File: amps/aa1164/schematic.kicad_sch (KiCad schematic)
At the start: 95 parts, among them SW1 SPST, SW2 SPDT

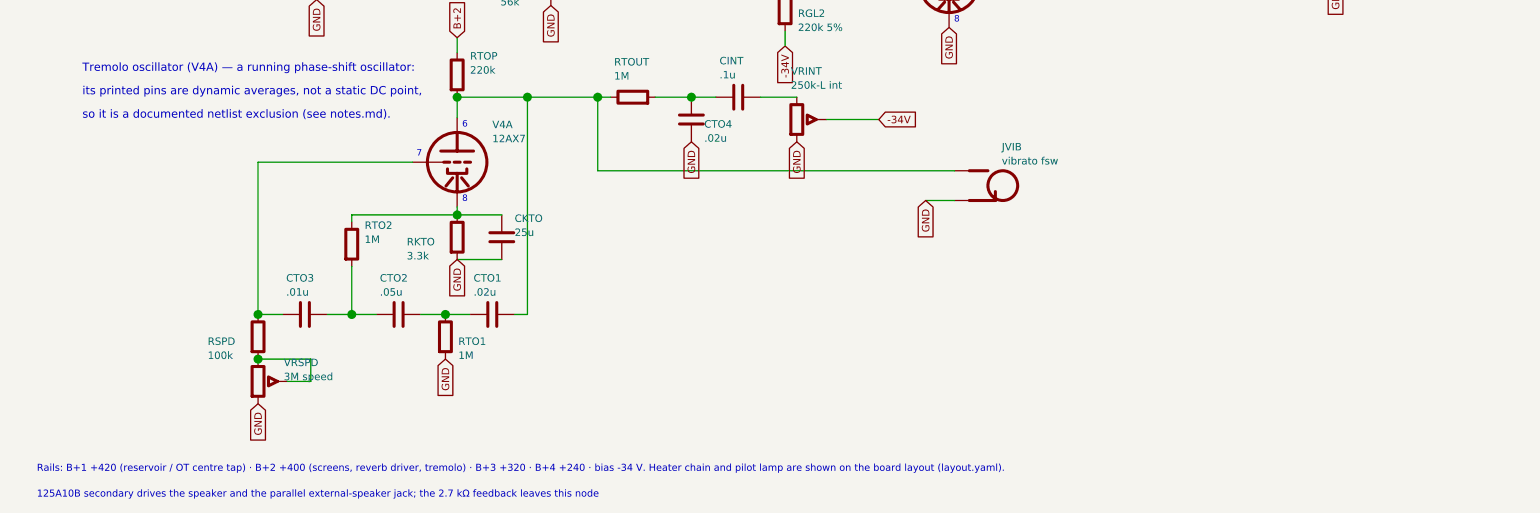
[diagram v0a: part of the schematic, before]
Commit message: Fix: schematic sheet notes no longer name repository files
Thirty-seven committed sheets rendered footnotes and section notes such as
"Heaters and PT primary omitted — see netlist.cir and meta.yaml" or
"excluded from netlist.cir (notes.md)" to visitors through KiCanvas. The
prose sweeps never counted sheets. Rewritten in the site's own words — the
netlist, the sources list, the circuit story, the parts list, the board
drawing — in 59 strings across 33 draw scripts, keeping every technical
claim as it was; the three tone sheets (6G4, 6G5, 6G6-B) are under repair
elsewhere and keep theirs for now. The sweep touched only strings passed to
the sheet's note, text, caption and footnote calls, never a path or a value.

Gates: check_schematics 40/0, connectivity 0 isolated pins;
verify_schematic_nets 40 clean; only the regenerated sheets and their served
copies changed.

Co-Authored-By: Claude Fable 5.1 <noreply@anthropic.com>
Claude-Session: https://claude.ai/code/session_01KBMfdh37HmCL2iWcBiL5J1
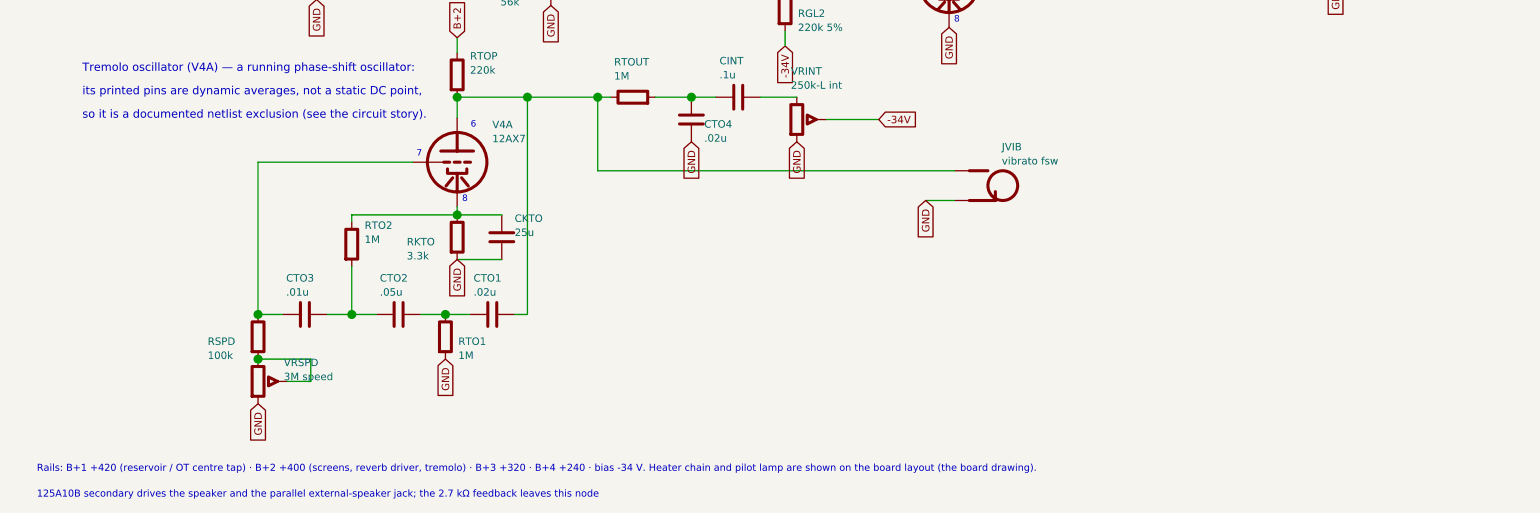
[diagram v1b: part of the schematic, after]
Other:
- note added: "Rails: B+1 +420 (reservoir / OT centre tap) · B+2 +400 (screens, reverb driver, tremolo) · B+3 +320 · B+4 +240 · bias -34 V. Heater chain and pilot lamp are shown on the board layout (the board drawing)."
- note added: "so it is a documented netlist exclusion (see the circuit story)."
- note removed: "Rails: B+1 +420 (reservoir / OT centre tap) · B+2 +400 (screens, reverb driver, tremolo) · B+3 +320 · B+4 +240 · bias -34 V. Heater chain and pilot lamp are shown on the board layout (layout.yaml)."
- note removed: "so it is a documented netlist exclusion (see notes.md)."
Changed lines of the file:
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@@
   (text "its printed pins are dynamic averages, not a static DC point," (at 20.4724 222.75 0)
     (effects (font (size 1.4 1.4)) (justify left)))
-  (text "so it is a documented netlist exclusion (see notes.md)." (at 20.4724 226.75 0)
+  (text "so it is a documented netlist exclusion (see the circuit story)." (at 20.4724 226.75 0)
     (effects (font (size 1.4 1.4)) (justify left)))
   (symbol (lib_id "cx:TRIODE") (at 84.4724 234.75 0) (unit 1)
@@
   (text "8" (at 169.322 210.465 0)
     (effects (font (size 1.1 1.1)) (justify left)))
-  (text "6" (at 85.3224 228.4 0)
+  (text "6" (at 86.7724 228.4 0)
     (effects (font (size 1.1 1.1)) (justify left)))
   (text "7" (at 77.5252 233.35 0)
@@
   (text "8" (at 85.3224 241.1 0)
     (effects (font (size 1.1 1.1)) (justify left)))
-  (text "Rails: B+1 +420 (reservoir / OT centre tap) · B+2 +400 (screens, reverb driver, tremolo) · B+3 +320 · B+4 +240 · bias -34 V. Heater chain and pilot lamp are shown on the board layout (layout.yaml)." (at 12.7 287.148 0)
+  (text "Rails: B+1 +420 (reservoir / OT centre tap) · B+2 +400 (screens, reverb driver, tremolo) · B+3 +320 · B+4 +240 · bias -34 V. Heater chain and pilot lamp are shown on the board layout (the board drawing)." (at 12.7 287.148 0)
     (effects (font (size 1.2 1.2)) (justify left)))
   (text "125A10B secondary drives the speaker and the parallel external-speaker jack; the 2.7 kΩ feedback leaves this node" (at 12.7 291.548 0)

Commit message: Fix: state the datasheet unit on 17 dual-triode sections whose sheets printed the other half's pin numbers
The sheet-vs-board gate reported these sockets as SECTION-SWAP; the
2026-09-10 source-read triage found the BOARD right on every one of them
(and both surfaces wrong on the 5G9 tremolo bottle). Each sheet had
lettered the section on the default map (A -> unit 1 -> pins 6/7/8) where
the factory drawing puts that stage on 1/2/3. The draw scripts now state
`unit=` on both halves, with the source cited beside the call, so the
printed socket numbers are the factory's:

- 5f4 V3: driver V3A -> 1/2/3, cathodyne V3B -> 6/7/8
  (crop 5f4-V3-layout-trace.png: +213 V driver plate -> pin 1, +270 V -> 6)
- 5f8a V3: 82k half V3A -> 1/2/3, 100k half V3B -> 6/7/8
  (crop 5f8a-V3-layout-trace.png: +225 -> 6, +19 -> 2, +28.5 -> 8)
- 6161 V1: channel 1 V1A -> 1/2/3 (crop 6161-V1-ch1.png prints 1/2/3);
  6161 V2: 1 MEG-grid half V2A -> 1/2/3, paraphase V2B -> 6/7/8
  (crop 6161-V2.png / 6161-V2-right.png)
- 6g3 V3: 82k half V3A -> 1/2/3 (crop 6g3-V3-layout-wires.png: +230 -> 1,
  +225 -> 6, +20 -> 7)
- aa1164 V3: recovery V3A -> 1/2/3, mixer V3B -> 6/7/8
  (crops aa1164-V3A-recovery-schem.png, aa1164-V3B-mixer-schem.png)
- aa864-bassman V1/V2: input stages 2/1/3, second stages 7/6/8; V4: the
  .1/500 pF-fed 82k half 2/1/3 (crops aa864-V1A-input.png,
  aa864-V1B-second.png, aa864-V2A-input.png, aa864-V2B-second.png,
  aa864-V4-PI.png)
- ab165 V1/V2/V4: same pattern (crops ab165-V1A-input.png,
  ab165-V1B-second.png, ab165-V2A-input.png, ab165-V2B-second.png,
  ab165-V4-PI.png)
- ab763-super V1/V2: slope-plate +270 V -> pin 1 (input stage), .047
  plate -> 6 (crops ab763-super-V1-layout-sh.png, ab763-super-V2-layout-sh.png)
- dr103 V2/V3: gain stages 6/7/8, cathode followers 1/2/3 (crops
  dr103-V2-huss.png, dr103-V3-huss.png — the Huss redraw, not a factory
  print; noted in the script)
- 5g9 V3: oscillator V3A -> 1/2/3, follower V3B -> 6/7/8 (crops
  5g9-V3-strap71-zoom.png, 5g9-V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
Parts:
- V3A: Basing_unit (none) -> 2
- V3B: Basing_unit (none) -> 1
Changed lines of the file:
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@@
     (in_bom yes) (on_board yes)
     (property "Reference" "V3A" (at 150.472 98.35 0) (effects (font (size 1.27 1.27)) (justify left)))
-    (property "Value" "12AX7" (at 150.472 100.75 0) (effects (font (size 1.27 1.27)) (justify left))))
+    (property "Value" "12AX7" (at 150.472 100.75 0) (effects (font (size 1.27 1.27)) (justify left)))
+    (property "Basing_unit" "2" (at 150.472 103.15 0) (effects (font (size 1.27 1.27)) hide)))
   (wire (pts (xy 132.472 104.75) (xy 136.852 104.75))
     (stroke (width 0) (type default)))
@@
     (in_bom yes) (on_board yes)
     (property "Reference" "V3B" (at 66.4724 176.35 0) (effects (font (size 1.27 1.27)) (justify left)))
-    (property "Value" "12AX7" (at 66.4724 178.75 0) (effects (font (size 1.27 1.27)) (justify left))))
+    (property "Value" "12AX7" (at 66.4724 178.75 0) (effects (font (size 1.27 1.27)) (justify left)))
+    (property "Basing_unit" "1" (at 66.4724 181.15 0) (effects (font (size 1.27 1.27)) hide)))
   (wire (pts (xy 44.4724 182.75) (xy 52.8524 182.75))
     (stroke (width 0) (type default)))
@@
   (text "3" (at 55.3224 133.1 0)
     (effects (font (size 1.1 1.1)) (justify left)))
-  (text "6" (at 145.322 98.4 0)
-    (effects (font (size 1.1 1.1)) (justify left)))
-  (text "7" (at 137.525 103.35 0)
-    (effects (font (size 1.1 1.1)) (justify left)))
-  (text "8" (at 145.322 111.1 0)
-    (effects (font (size 1.1 1.1)) (justify left)))
-  (text "1" (at 61.3224 176.4 0)
-    (effects (font (size 1.1 1.1)) (justify left)))
-  (text "2" (at 53.5252 181.35 0)
-    (effects (font (size 1.1 1.1)) (justify left)))
-  (text "3" (at 61.3224 189.1 0)
+  (text "1" (at 145.322 98.4 0)
+    (effects (font (size 1.1 1.1)) (justify left)))
+  (text "2" (at 137.525 103.35 0)
+    (effects (font (size 1.1 1.1)) (justify left)))
+  (text "3" (at 145.322 111.1 0)
+    (effects (font (size 1.1 1.1)) (justify left)))
+  (text "6" (at 61.3224 176.4 0)
+    (effects (font (size 1.1 1.1)) (justify left)))
+  (text "7" (at 53.5252 181.35 0)
+    (effects (font (size 1.1 1.1)) (justify left)))
+  (text "8" (at 61.3224 189.1 0)
     (effects (font (size 1.1 1.1)) (justify left)))
   (text "1" (at 101.322 176.4 0)

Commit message: Fix: 17 bias rectifiers and six HT diodes drawn backwards; the 6G6-B and 6G4 bias rows as their drawings show; AA1164 V4 units
Rectifier polarity has no gate. The netlists model every supply as an ideal
source, the sheet-vs-board check treats a two-terminal part as unordered, and
the boards' `cathode:` fields were copied from the sheets. Measured over all
68 diodes on 40 sheets: 18 negative-bias rectifiers had the cathode on the
negative node (a diode that way round would charge the node POSITIVE), and all
six 6G6-B HT diodes pointed away from B+. The printed negative bias on each of
those sheets falsifies the drawn orientation; the nine bias rectifiers already
right (AA1164, AA864, AB165, B15N, DR103, JTM100, M1959, M2204, 6G6-B) show
the idiom. Flipped: 5E4-A, 5E5-A, 5E6-A, 5F10, 5F4, 5F6, 5F6-A, 5F8-A, 5G9,
6G2, 6G3, 6G4, 6G5, AA964, AB763, AB763 Super, AB763 Twin, JTM45 (the
M1987's is with the Marshall board repair) and the 6G6-B's DR1-DR6. The
5F8-A board, which had copied its sheet, has the band moved to the tap side;
the other boards' bands are with the board-repair wave. A gate is next.

6G6-B bias. E-FB (6431x3364): the 1K 1W rises from TR1's SECOND secondary
terminal, a bias tap between the upper HT end and the grounded centre tap,
to the diode's + end. The sheet fed the diode from the HT end with the 1K
after it. T1 now carries its tap pin and the row reads tap -> 1K -> diode ->
-54 V. (The triage had read "HT end"; the native crop shows the tap.)

6G4 bias. A-FJ, read natively: tap -> rectifier -> 8 uF -> 10K -> the -55 V
node, which carries a second 8 uF and the 56K to ground as a bleeder. The
sheet fed the rectifier from an HT end, drew the 56K in series and carried
one capacitor. CBIAS2 joins the parts list, and RBIAS1's role now says
bleeder.

AA1164 V4. The K-FD sheet prints the phase inverter 7/6/8 and the tremolo
oscillator 2/1/3 (5554x4346); the sheet had them the other way round.

Gates: check_schematics 40/0 (+selftest), verify_schematic_nets 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
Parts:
- V4A: Basing_unit (none) -> 2
- V4B: Basing_unit (none) -> 1
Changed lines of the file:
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@@
     (in_bom yes) (on_board yes)
     (property "Reference" "V4B" (at 106.472 176.35 0) (effects (font (size 1.27 1.27)) (justify left)))
-    (property "Value" "12AX7" (at 106.472 178.75 0) (effects (font (size 1.27 1.27)) (justify left))))
+    (property "Value" "12AX7" (at 106.472 178.75 0) (effects (font (size 1.27 1.27)) (justify left)))
+    (property "Basing_unit" "1" (at 106.472 181.15 0) (effects (font (size 1.27 1.27)) hide)))
   (junction (at 86.4724 182.75) (diameter 1.54) (color 0 0 0 0))
   (wire (pts (xy 86.4724 182.75) (xy 92.8524 182.75))
@@
     (in_bom yes) (on_board yes)
     (property "Reference" "V4A" (at 90.4724 228.35 0) (effects (font (size 1.27 1.27)) (justify left)))
-    (property "Value" "12AX7" (at 90.4724 230.75 0) (effects (font (size 1.27 1.27)) (justify left))))
+    (property "Value" "12AX7" (at 90.4724 230.75 0) (effects (font (size 1.27 1.27)) (justify left)))
+    (property "Basing_unit" "2" (at 90.4724 233.15 0) (effects (font (size 1.27 1.27)) hide)))
   (wire (pts (xy 84.4724 227.13) (xy 84.4724 223.65))
     (stroke (width 0) (type default)))
@@
   (text "8" (at 61.3224 189.1 0)
     (effects (font (size 1.1 1.1)) (justify left)))
-  (text "1" (at 101.322 176.4 0)
-    (effects (font (size 1.1 1.1)) (justify left)))
-  (text "2" (at 93.5252 181.35 0)
-    (effects (font (size 1.1 1.1)) (justify left)))
-  (text "3" (at 101.322 189.1 0)
+  (text "6" (at 101.322 176.4 0)
+    (effects (font (size 1.1 1.1)) (justify left)))
+  (text "7" (at 93.5252 181.35 0)
+    (effects (font (size 1.1 1.1)) (justify left)))
+  (text "8" (at 101.322 189.1 0)
     (effects (font (size 1.1 1.1)) (justify left)))
   (text "3" (at 169.322 159.765 0)
@@
   (text "8" (at 169.322 210.465 0)
     (effects (font (size 1.1 1.1)) (justify left)))
-  (text "6" (at 86.7724 228.4 0)
-    (effects (font (size 1.1 1.1)) (justify left)))
-  (text "7" (at 77.5252 233.35 0)
-    (effects (font (size 1.1 1.1)) (justify left)))
-  (text "8" (at 85.3224 241.1 0)
+  (text "1" (at 86.7724 228.4 0)
+    (effects (font (size 1.1 1.1)) (justify left)))
+  (text "2" (at 77.5252 233.35 0)
+    (effects (font (size 1.1 1.1)) (justify left)))
+  (text "3" (at 85.3224 241.1 0)
     (effects (font (size 1.1 1.1)) (justify left)))
   (text "Rails: B+1 +420 (reservoir / OT centre tap) · B+2 +400 (screens, reverb driver, tremolo) · B+3 +320 · B+4 +240 · bias -34 V. Heater chain and pilot lamp are shown on the board layout (the board drawing)." (at 12.7 287.148 0)

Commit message: Fix: the 6G5's rectifier was connected to nothing; 17 sheets shorted the mains by naming both leads alike
6G5 power supply. The sheet drew four diodes as a "silicon bridge" whose
HT_A/HT_B labels stopped 6 mm short of their wires. D1/D2's anodes sat on
the tremolo's cathode node (a tremolo wire's end touched the old diode
stub), D3/D4 ran from ground to the reservoir, and TR1's centre tap floated
under an open-pin waiver whose stated reason was the bridge itself.
A-FJ (Schematic Heaven 2153x1437, read enlarged): each HT end of TR1 runs
through a leg of three silicon diodes, every + (cathode) toward the +460 V
reservoir; the centre tap is grounded; TR1's second secondary terminal is a
bias tap feeding the 6G4's network part for part: rectifier, 8-150, 10K,
then 8-150 and a 56K bleeder at the -55 V line. Redrawn as the drawing
shows: D1-D6, TR1 with its tap pin, the centre tap to ground, the bias
network (CBIAS 25 uF -> 8 uF; RBIAS2, CBIAS2, RBIAS1 added), the waiver
deleted, and the notes, meta, netlist header and parts list no longer say
bridge. Not yet carried: the drawing's second 20-600 at the reservoir and
the standby switch (this sheet omits chassis switches by its own note);
and the tremolo ladder still runs through the transformer's corner of the
sheet, a layout clash rather than a connection, queued for its own redraw.

Mains. Two global labels with one name are one net. 16 of 24 power
transformers on the sheets carried a label named MAINS on both primary
leads, so the winding's two pins were one net: 5E4-A, 5E5-A, 5F4, 5G9,
6161, 6G2, 6G3, 6G4, AA1164, AA764, AA764-Vibro, AA964, AB763, AB763
Super, AB763 Twin, GA-40. The 6G5's loop ran from one MAINS label through
switch, fuse and winding back to the same name. No gate models the primary,
so a copy-pasted idiom did this. The second lead is now MAINS N, the AC15's
idiom; the AA1164's and AA964's second AC row, drawn under the first row's
name, is the neutral. The death and across-the-line caps stay on the le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
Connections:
- net AC LINE: no longer CDEATH.1
- net MAINS: no longer TR1.2 (PRI_2)
- new net MAINS N: CDEATH.1, TR1.2 (PRI_2)
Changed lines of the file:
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@@
   (wire (pts (xy 215.582 53.83) (xy 211.582 53.83))
     (stroke (width 0) (type default)))
-  (global_label "MAINS" (shape input) (at 211.582 53.83 180)
+  (global_label "MAINS N" (shape input) (at 211.582 53.83 180)
     (effects (font (size 1.27 1.27)) (justify right)))
   (wire (pts (xy 233.362 43.67) (xy 237.362 43.67))
@@
   (global_label "MAINS" (shape input) (at 300.472 140.75 0)
     (effects (font (size 1.27 1.27)) (justify left)))
-  (global_label "AC LINE" (shape input) (at 260.472 152.75 180)
+  (global_label "MAINS N" (shape input) (at 260.472 152.75 180)
     (effects (font (size 1.27 1.27)) (justify right)))
   (symbol (lib_id "cx:C") (at 274.472 152.75 90) (unit 1)

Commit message: Fix: AA1164 tremolo ladder and Intensity return drawn as the K-FD sheet draws them
- The phase-shift ladder was scrambled. The sheet had the Speed network on the
  grid node, the vibrato-pedal jack on the plate tee, a 1 M to ground where the
  Speed network belongs, and the middle cap lettered .05. The drawing (read at
  5554 x 4346): plate -> .02 -> Speed node (3M-RA + 100k to ground) -> .01 ->
  pedal node (jack; 1M to the cathode) -> .01 -> grid (1M to ground).
- CTO2 is 0.01 uF, not 0.05 uF (sheet and bom.yaml).
- The Intensity control's far end was grounded and its wiper shared one net
  with the bias filter node. The drawing runs the track from the 0.1 coupler
  to the filter node (22k, 25 uF, rectifier) and letters -34V on the wiper's
  line to the two 220k leaks. The filter node now has its own label.
- Sheet only. The oscillator is excluded from netlist.cir and the -34 V line is
  an ideal source there, so no gated value moves.

Co-Authored-By: Claude Opus 5 (1M context) <noreply@anthropic.com>
Claude-Session: https://claude.ai/code/session_01KBMfdh37HmCL2iWcBiL5J1
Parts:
- removed RSPD: 100k, symbol cx:R
- removed VRINT: 250k-L int, symbol cx:POT
- removed VRSPD: 3M speed, symbol cx:POT
- added CTO3: .01u, symbol cx:C
- added JVIB: vibrato fsw, symbol cx:JACK
- added RTO2: 1M, symbol cx:R
- RSPD: renamed from RTO2; value 1M -> 100k
- VRINT: renamed from JVIB; value vibrato fsw -> 250k-L int; symbol cx:JACK -> cx:POT
- VRSPD: renamed from CTO2; value .05u -> 3M speed; symbol cx:C -> cx:POT
- renumbered CTO3 to CTO2
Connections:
- net -34V: now also VRINT.2 (W); no longer CB3.1, DB1.1 (A), RB2.1
- net GND: now also RSPD.2, JVIB.2 (S); no longer VRINT.2 (S)
- net at CTO2.1: now also CTO3.2, JVIB.1 (T), RTO2.2; no longer V4A.2 (G)
- net at CTO2.2, VRSPD.1: now also CTO1.2, VRSPD.2 (W); no longer RSPD.2
- net at CINT.2: now also VRINT.1
- net at RTOP.2, RTOUT.1, V4A.1 (P): now also CTO1.1; no longer CTO1.2, VRINT.1 (T)
- net at CKTO.1, RKTO.1, V4A.3 (K): now also RTO2.1; no longer RSPD.1
- new net: CTO3.1, RTO1.1, V4A.2 (G)
- new net: RSPD.1, VRSPD.3
- new net BIAS FILTER: CB3.1, DB1.1 (A), RB2.1, VRINT.3
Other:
- note added: "Bias supply — 100 k feed off the HT winding, silicon rectifier, 25 µF can, 22 k bleeder; the Intensity control's track ends here and its wiper is the -34 V line"
- note removed: "Bias supply — 100 k feed off the HT winding, silicon rectifier, 25 µF can, 22 k bleeder → -34 V"
- moved on the sheet: CTO2, RSPD
